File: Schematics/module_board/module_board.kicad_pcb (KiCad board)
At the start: 2 copper layers, 30 x 30 mm, 33 parts, among them J1 Conn_01x01_Male, J11 Conn_01x01_Male, J12 Conn_01x01_Male, J13 Conn_01x01_Male, J14 Conn_01x01_Male, J15 Conn_01x01_Male, J16 Conn_01x01_Male, J17 Conn_01x01_Male, J2 Conn_01x01_Male, J3 Conn_01x01_Male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

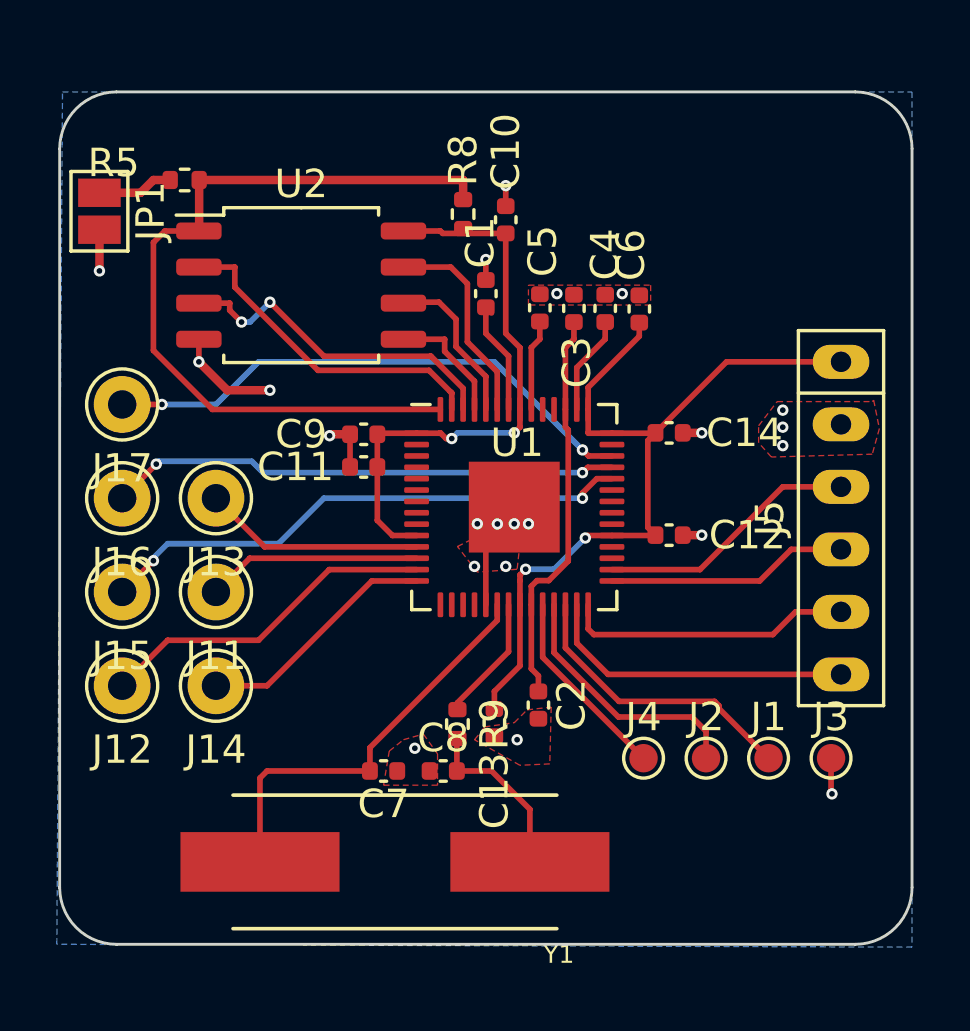
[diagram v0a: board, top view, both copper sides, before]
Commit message: Fixed copper plates
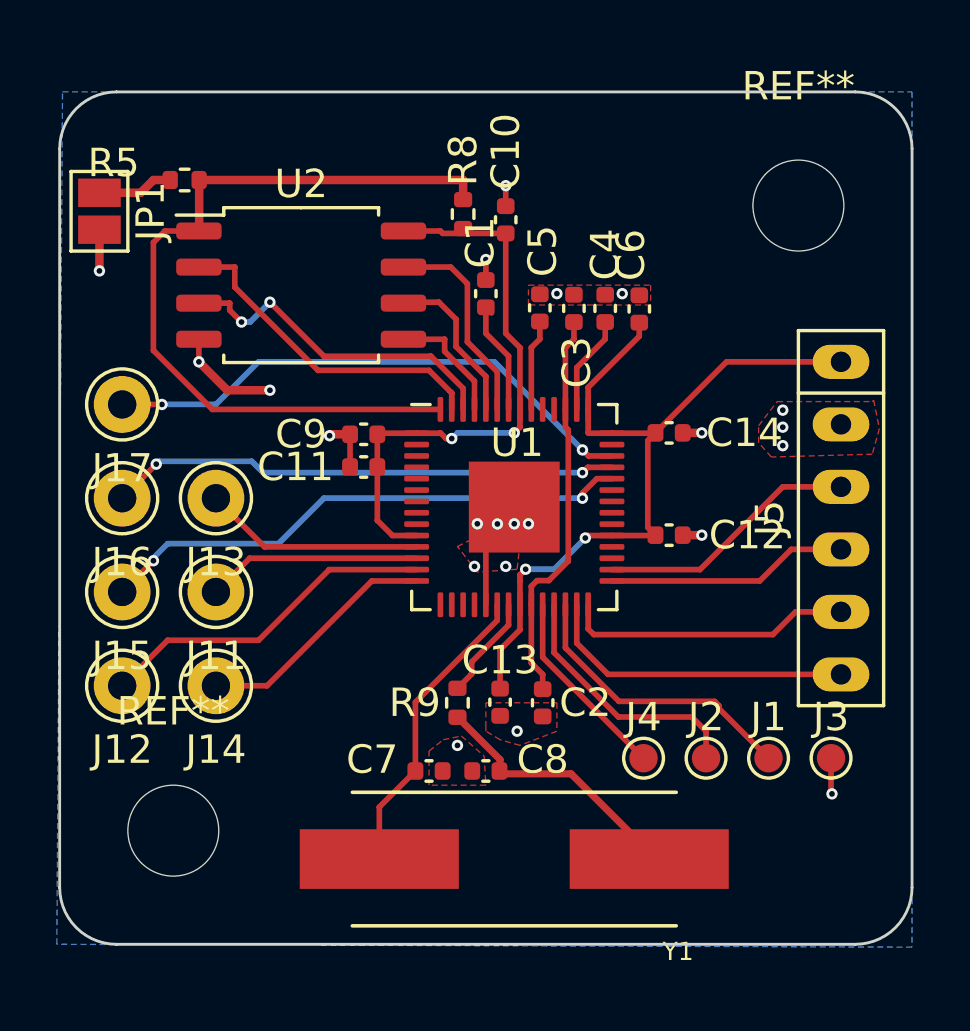
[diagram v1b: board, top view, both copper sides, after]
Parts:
- added REF**: MountingHole_3.2mm_M3, MountingHole:MountingHole_3.2mm_M3, F.Cu at (149.0, 101.0)
- added REF**: MountingHole_3.2mm_M3, MountingHole:MountingHole_3.2mm_M3, F.Cu at (171.0, 79.0)
- moved Y1 4.20 mm to (161.0, 102.0)
- moved C7 1.60 mm to (158.0, 98.9)
- moved C8 1.50 mm to (160.0, 98.9)
- moved R9 0.75 mm to (159.0, 96.5)
- moved C13 0.75 mm to (160.5, 96.5)
- moved C2 0.17 mm to (162.0, 96.5)
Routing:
- net /XTAL_IN: track 14.6 -> 10.7 mm
- net Net-(C8-Pad2): track 6.13 -> 9.23 mm
- net +3V3: track 56.1 -> 55.3 mm
- net /XTAL_OUT: track 4.44 -> 3.69 mm

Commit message: Adjusted Module Board, fixed majority of DRC errors/warnings
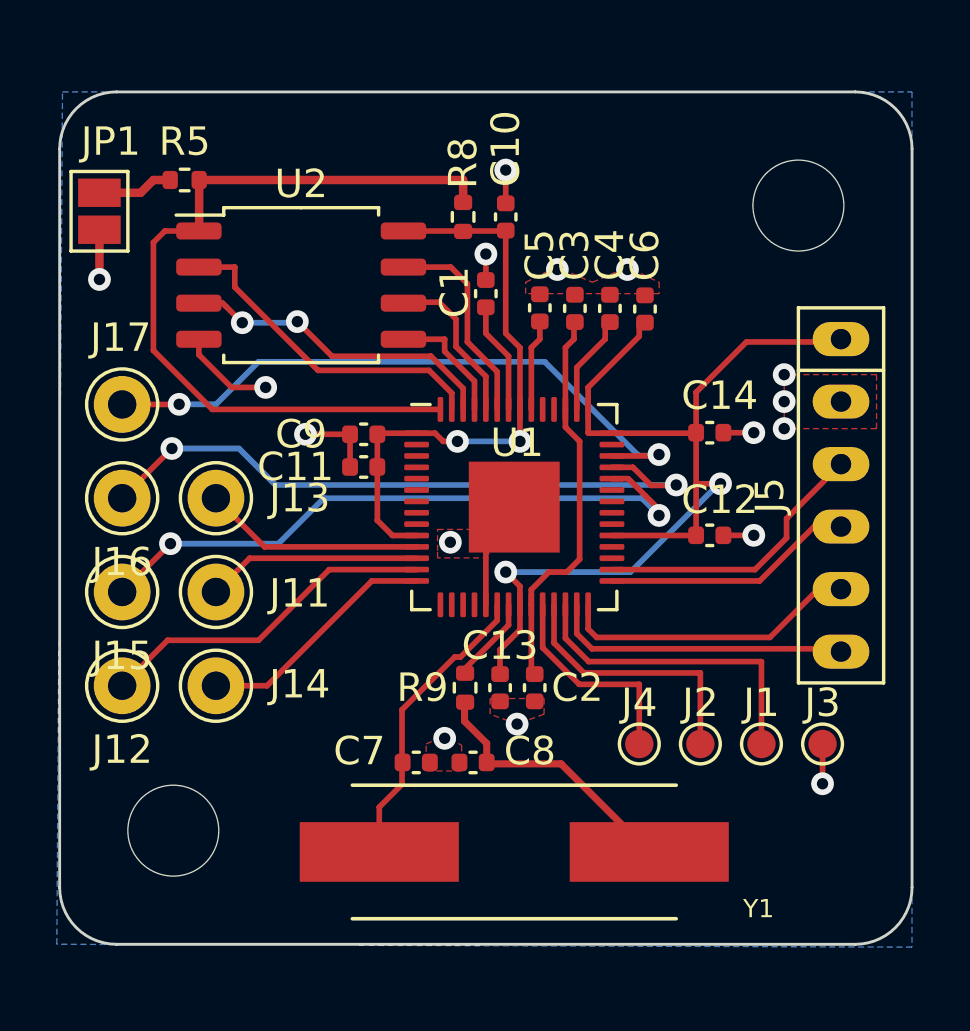
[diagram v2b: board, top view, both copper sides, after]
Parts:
- moved C12 1.43 mm to (167.9, 90.6)
- moved C14 1.43 mm to (167.9, 87.0)
- moved J5 0.80 mm to (172.5, 89.2)
- moved C2 0.60 mm to (161.7, 96.0)
- moved R9 0.59 mm to (159.3, 96.0)
- moved J3 0.58 mm to (171.8, 98.0)
- moved J1 0.56 mm to (169.7, 98.0)
- moved C7 0.54 mm to (157.6, 98.6)
- moved C8 0.54 mm to (159.6, 98.6)
- moved J2 0.54 mm to (167.6, 98.0)
- moved J4 0.52 mm to (165.4, 98.0)
- moved C13 0.51 mm to (160.5, 96.0)
- moved Y1 0.25 mm to (161.0, 101.8)
- moved C6 0.20 mm to (165.6, 82.6)
- moved C4 0.17 mm to (164.4, 82.6)
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- renumbered REF** to hello
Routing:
- net +3V3: track 55.3 -> 62.9 mm
- net /GPIO27_ADC1: track 18.0 -> 23.3 mm
- net /GPIO26_ADC0: track 19.1 -> 22.8 mm
- net /GPIO28_ADC2: track 19.2 -> 22.6 mm
- net GND: track 15.0 -> 17.5 mm, vias 22 -> 16
- net /RX: track 11.1 -> 9.78 mm
- net /RESET_N: track 10.3 -> 11.3 mm
- net /TX: track 9.27 -> 10.0 mm
- net /QSPI_SD2: track 12.0 -> 11.3 mm
- net /SWCLK: track 6.87 -> 7.55 mm
- net /XTAL_OUT: track 3.69 -> 3.04 mm
